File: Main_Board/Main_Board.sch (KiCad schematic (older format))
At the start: 66 parts, among them J1 Conn_01x06, J10 HR-SR04_L_CONN, J11 12V_OUT, J12 BATT_REG_IN, J13 LED_CONN, J14 PD_CONN, J2 Conn_01x06, J3 Conn_01x06, J4 BATT_IN, J5 Conn_02x08_Row_Letter_First, J6 MAGN_CONN, J7 OLED_CONN, J8 Conn_02x07_Counter_Clockwise, J9 HR-SR04_R_CONN, Q1 Q_PMOS_GDS, Q2 Q_PMOS_GDS, SW1 SW_SPST, SW2 SW_Push, SW3 EN, SW4 SW_SPST, U1 TEENSY_4_1_MASTER, U2 TEENSY_4_1_SLAVE, U3 G2-24v13, U4 G2-24v13, U5 G2-24v13, U6 SiC467ED

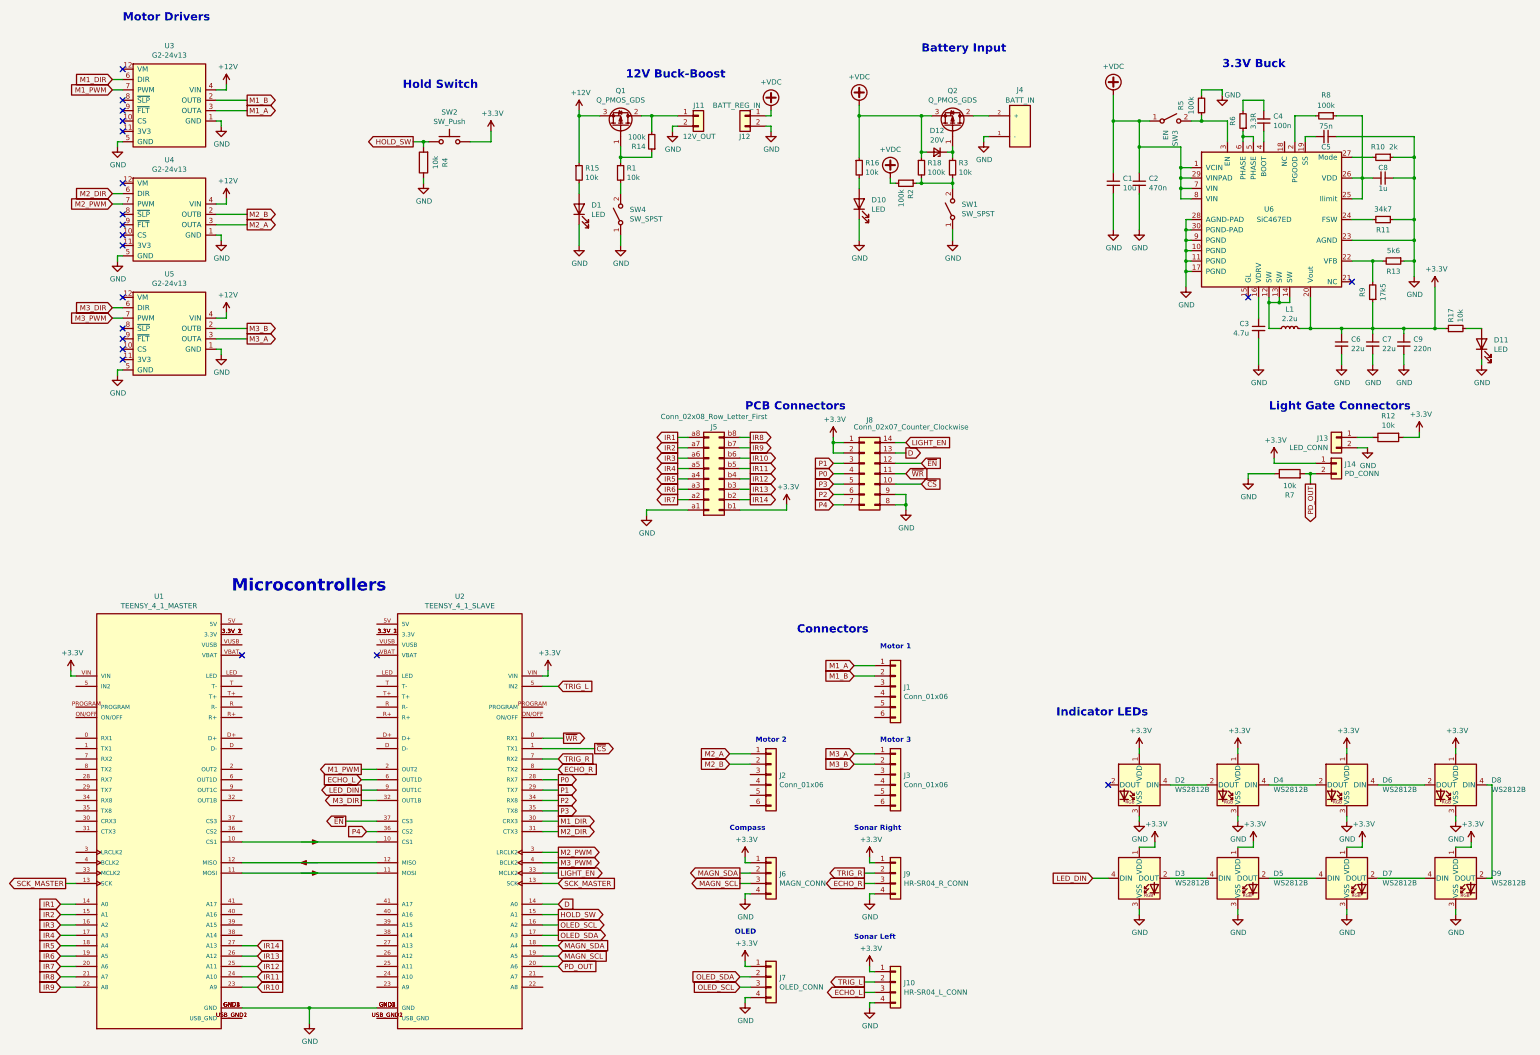
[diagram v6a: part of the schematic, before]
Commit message: Started Main PCB Drawing
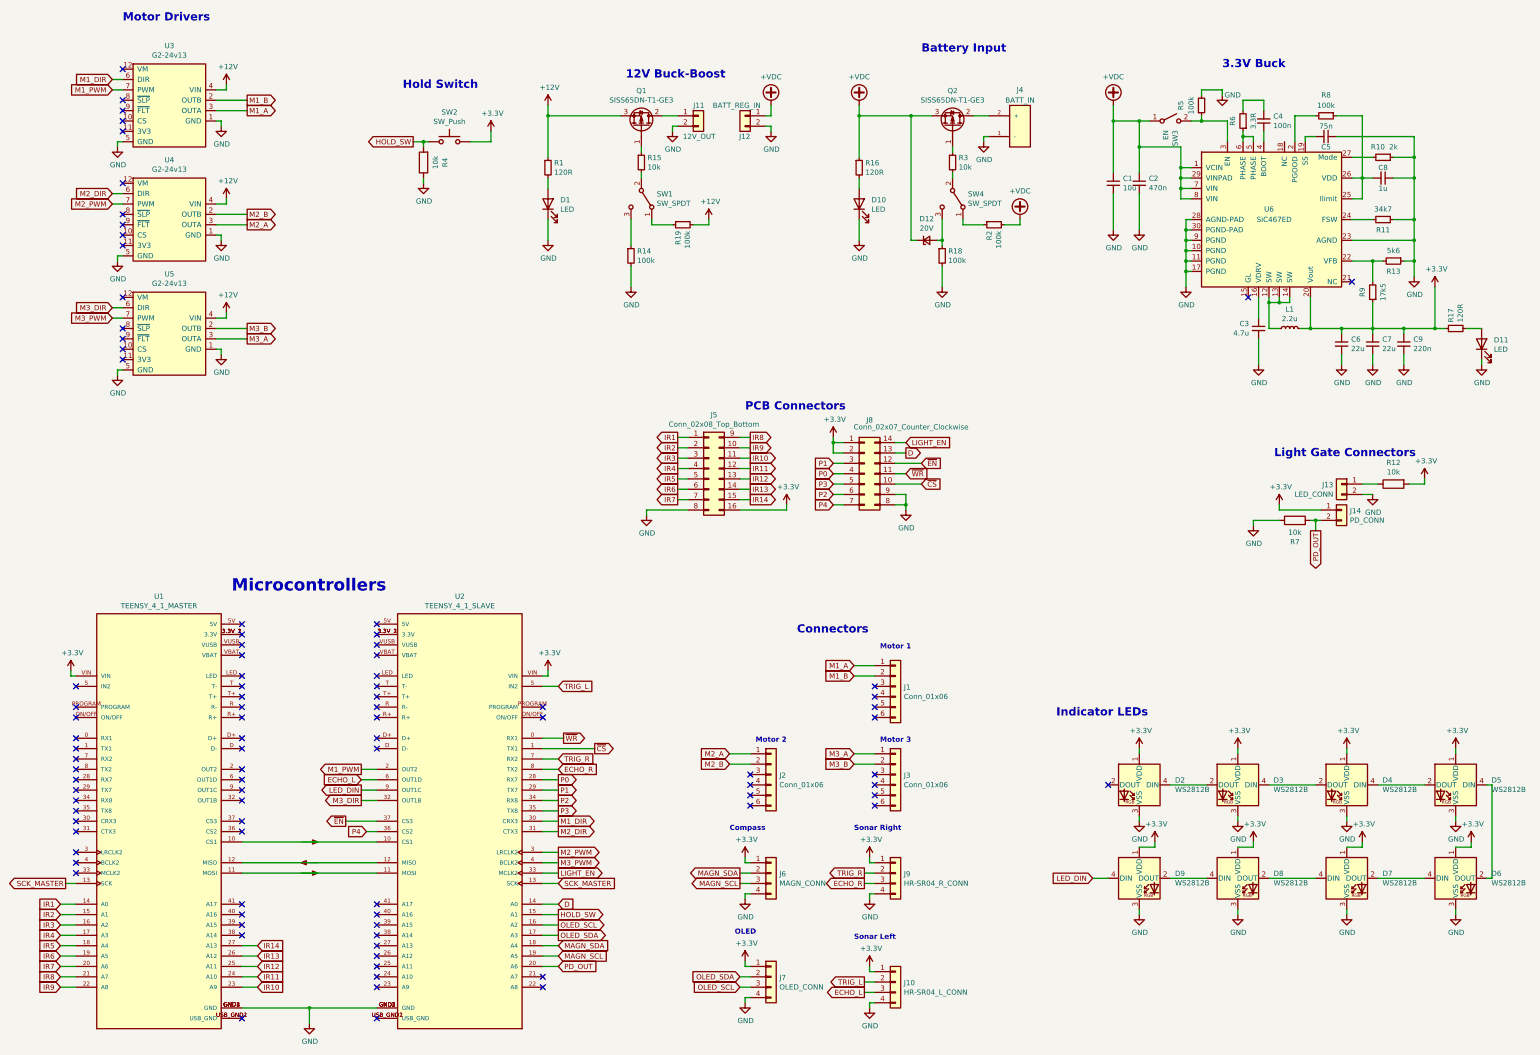
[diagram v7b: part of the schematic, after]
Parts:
- removed J5: Conn_02x08_Row_Letter_First, Connector_Hirose:Hirose_DF11-16DP-2DSA_2x08_P2.00mm_Vertical, symbol Connector_Generic:Conn_02x08_Row_Letter_First
- removed SW1, SW4: SW_SPST, symbol Switch:SW_SPST
- added J5: Conn_02x08_Top_Bottom, Connector_Hirose:Hirose_DF11-16DP-2DSA_2x08_P2.00mm_Vertical, symbol Connector_Generic:Conn_02x08_Top_Bottom
- added R19: 100k, Resistor_SMD:R_0603_1608Metric, symbol Device:R_Small
- added SW1, SW4: SW_SPDT, Main_Board:EG1218, symbol Switch:SW_SPDT
- D12: footprint (none) -> Diode_SMD:D_SOD-123
- J11, J12: footprint (none) -> Connector_Molex:Molex_Mini-Fit_Jr_5566-04A_2x02_P4.20mm_Vertical
- Q1, Q2: value Q_PMOS_GDS -> SISS65DN-T1-GE3; footprint (none) -> Package_SO:Vishay_PowerPAK_1212-8_Single
- R1: value 10k -> 120R; footprint (none) -> Resistor_SMD:R_0603_1608Metric
- R10, R11, R14, R18, R2, R5, R6, R8: footprint (none) -> Resistor_SMD:R_0603_1608Metric
- R12, R13, R15, R3, R4, R7, R9: footprint (none) -> Resistor_SMD:R_0805_2012Metric
- R16, R17: value 10k -> 120R; footprint (none) -> Resistor_SMD:R_0805_2012Metric
- SW2, SW3: footprint (none) -> Main_Board:EG1218
- U3, U4, U5: footprint (none) -> Main_Board:G2-24v13
- U6: footprint (none) -> Main_Board:Vishay_PowerPAK_MLP55-27L_ThermalVias
- renumbered D4 to D3, D6 to D4, D8 to D5, D9 to D6, D5 to D8, D3 to D9
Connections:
- net +12V: now also R1.1, R19.2; no longer R15.1
- net +3V3: now also J5.16 (Pin_16)
- net +VDC: now also D12.1 (K); no longer D12.2 (A), R18.1
- net GND: now also R14.2, R18.2, J5.8 (Pin_8)
- net IR1: now also J5.1 (Pin_1)
- net IR10: now also J5.11 (Pin_11)
- net IR11: now also J5.12 (Pin_12)
- net IR12: now also J5.13 (Pin_13)
- net IR13: now also J5.14 (Pin_14)
- net IR14: now also J5.15 (Pin_15)
- net IR2: now also J5.2 (Pin_2)
- net IR3: now also J5.3 (Pin_3)
- net IR4: now also J5.4 (Pin_4)
- net IR5: now also J5.5 (Pin_5)
- net IR6: now also J5.6 (Pin_6)
- net IR7: now also J5.7 (Pin_7)
- net IR8: now also J5.9 (Pin_9)
- net IR9: now also J5.10 (Pin_10)
- net at Q2.1 (G), R3.1: no longer D12.1 (K)
- net at J11.1 (Pin_1), Q1.2 (D): no longer R14.2
- net at R1.2: now also D1.2 (A)
- net at R15.2: now also SW1.2 (B); no longer D1.2 (A)
- new net: R3.2, SW4.2 (B)
- new net: R2.1, SW4.1 (A)
- new net: D12.2 (A), R18.1, SW4.3 (C)
- new net: Q1.1 (G), R15.1
- new net: R14.1, SW1.3 (C)
- new net: R19.1, SW1.1 (A)
- no-connect marks 20 -> 93
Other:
- moved on the sheet: D12, J13, J14, R12, R18, R2, R3, R7

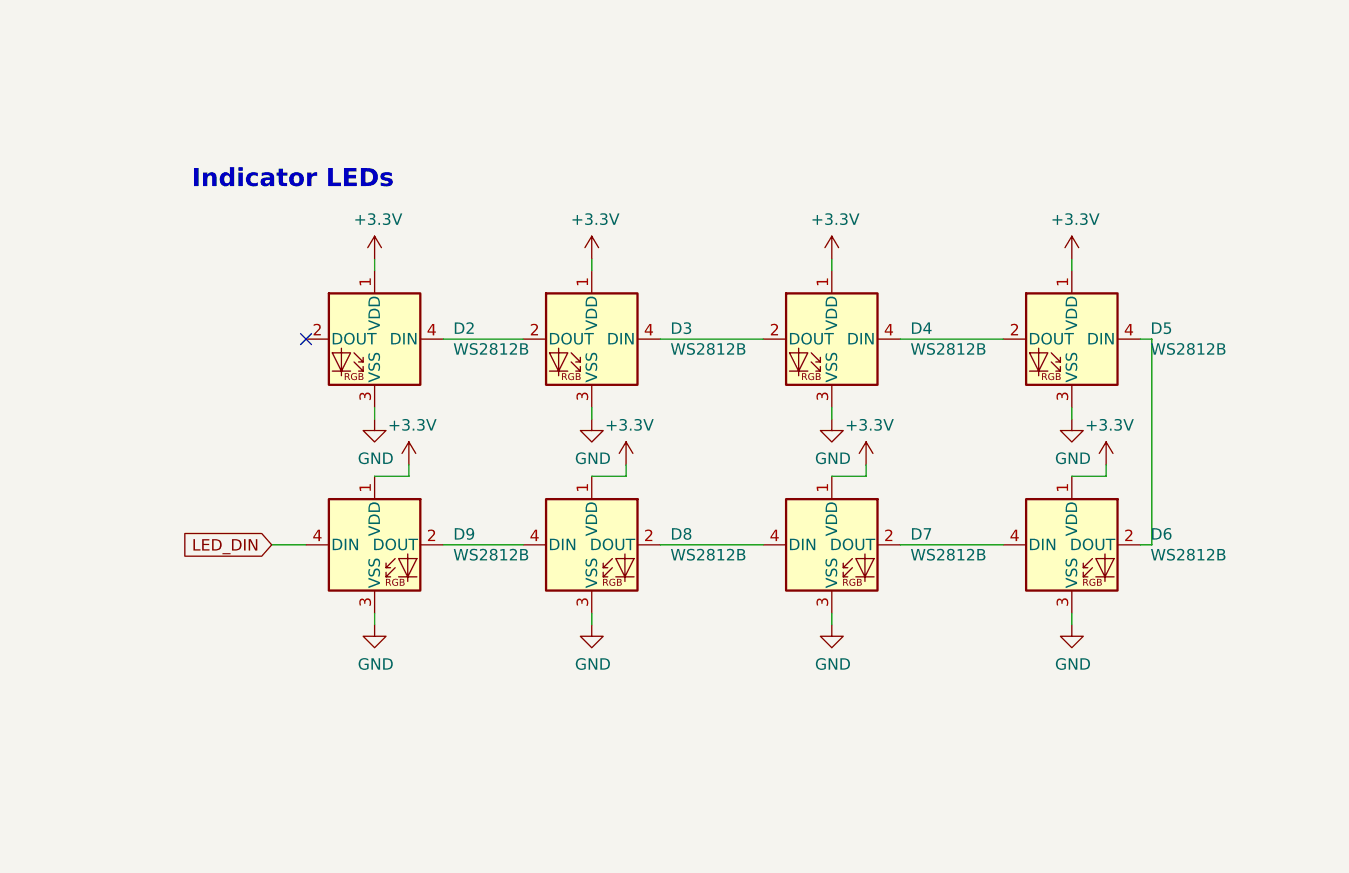
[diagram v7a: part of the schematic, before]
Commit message: Finished Power Planes and layout, started drawing traces [MAIN BOARD]
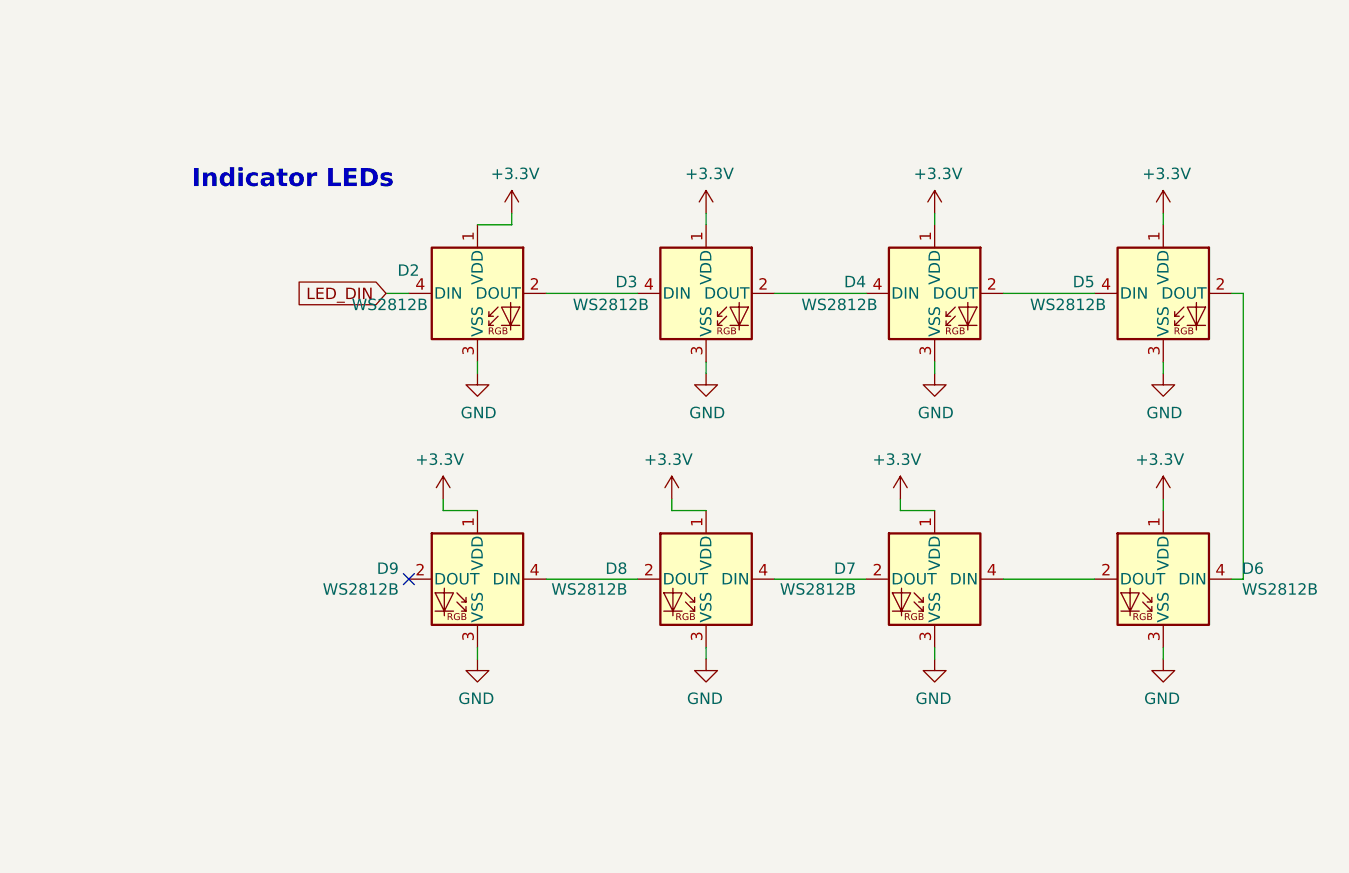
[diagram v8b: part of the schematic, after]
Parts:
- J4: footprint Main_Board:AMASS_XT60-M -> Main_Board:AMASS_XT60PW-M
- J7: footprint Connector_JST:JST_EH_B4B-EH-A_1x04_P2.50mm_Vertical -> Connector_PinSocket_2.54mm:PinSocket_1x04_P2.54mm_Vertical
- R16, R17: footprint Resistor_SMD:R_0805_2012Metric -> Resistor_SMD:R_0603_1608Metric
- SW2: footprint Main_Board:EG1218 -> Main_Board:EVP-BT2J4A000
- renumbered D6 to D2, D4 to D3, D2 to D4, D3 to D5, D5 to D6, D8 to D7, D9 to D8, D7 to D9
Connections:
- net LED_DIN: now also D2.4 (DIN); no longer D8.4 (DIN)
- net at D4.2 (DOUT): now also D5.4 (DIN)
- net at D4.4 (DIN): now also D3.2 (DOUT); no longer D5.2 (DOUT)
- net at D6.2 (DOUT): now also D7.4 (DIN); no longer D3.4 (DIN)
- net at D6.4 (DIN): now also D5.2 (DOUT); no longer D2.2 (DOUT)
- net at D9.2 (DOUT): no longer D2.4 (DIN)
- net at D8.2 (DOUT): now also D9.4 (DIN); no longer D7.4 (DIN)
- net at D7.2 (DOUT): now also D8.4 (DIN); no longer D9.4 (DIN)
- new net: D2.2 (DOUT), D3.4 (DIN)
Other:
- moved on the sheet: D2, D3, D4, D5, D6, D7, D8, D9
